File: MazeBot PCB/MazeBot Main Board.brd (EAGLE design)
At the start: 74.9 x 45.4 mm, 43 parts, among them IC1 7805TV, IC2 L298, Q1 16MHz

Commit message: Add mounting screw holes
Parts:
- moved MOT_R 1.27 mm to (64.8, 40.6)
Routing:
- net MOT2_R: track 51.3 -> 48.6 mm
- net MOT1_R: track 48.1 -> 47.6 mm
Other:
- board size 74.9 x 45.4 mm -> 76.2 x 45.4 mm
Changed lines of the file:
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@@
 <layer number="43" name="vRestrict" color="2" fill="10" visible="yes" active="yes"/>
 <layer number="44" name="Drills" color="7" fill="1" visible="no" active="yes"/>
-<layer number="45" name="Holes" color="7" fill="1" visible="no" active="yes"/>
+<layer number="45" name="Holes" color="7" fill="1" visible="yes" active="yes"/>
 <layer number="46" name="Milling" color="3" fill="1" visible="no" active="yes"/>
 <layer number="47" name="Measures" color="7" fill="1" visible="no" active="yes"/>
@@
 <board>
 <plain>
-<wire x1="0" y1="0" x2="74.91" y2="0" width="0" layer="20"/>
-<wire x1="74.91" y1="0" x2="74.91" y2="45.39" width="0" layer="20"/>
-<wire x1="74.91" y1="45.39" x2="0" y2="45.39" width="0" layer="20"/>
+<wire x1="0" y1="0" x2="76.18" y2="0" width="0" layer="20"/>
+<wire x1="76.18" y1="0" x2="76.18" y2="45.39" width="0" layer="20"/>
+<wire x1="76.18" y1="45.39" x2="0" y2="45.39" width="0" layer="20"/>
 <wire x1="0" y1="45.39" x2="0" y2="0" width="0" layer="20"/>
+<hole x="2.54" y="3.81" drill="3.5"/>
+<hole x="2.54" y="41.91" drill="3.5"/>
+<hole x="73.66" y="3.81" drill="3.5"/>
+<hole x="73.66" y="42.164" drill="3.5"/>
 </plain>
 <attributes>
@@
 <attribute name="NAME" x="6.27" y="37.64" size="1.27" layer="25" rot="R90"/>
 </element>
-<element name="MOT_R" library="adafruit" package="1X2-3.5MM" value="1X2-3.5MM" x="63.5" y="40.64" smashed="yes" rot="R180">
-<attribute name="NAME" x="67.39" y="43.64" size="1.27" layer="25" rot="R270"/>
+<element name="MOT_R" library="adafruit" package="1X2-3.5MM" value="1X2-3.5MM" x="64.77" y="40.64" smashed="yes" rot="R180">
+<attribute name="NAME" x="68.66" y="43.64" size="1.27" layer="25" rot="R270"/>
 </element>
 <element name="PWR_IN" library="adafruit" package="1X2-3.5MM" value="1X2-3.5MM" x="35.56" y="40.64" smashed="yes" rot="R180">
@@
 <contactref element="C11" pad="-"/>
 <contactref element="PWR_IN" pad="1"/>
-<polygon width="0.4064" layer="1" isolate="0.3048">
-<vertex x="0" y="45.72"/>
-<vertex x="0" y="0"/>
-<vertex x="74.93" y="0"/>
-<vertex x="74.93" y="44.45"/>
-<vertex x="74.93" y="45.72"/>
-</polygon>
-<polygon width="0.4064" layer="16" isolate="0.3048">
-<vertex x="0" y="45.72"/>
-<vertex x="0" y="0"/>
-<vertex x="74.93" y="0"/>
-<vertex x="74.93" y="45.72"/>
-</polygon>
 <via x="44.958" y="19.939" extent="1-16" drill="0.35"/>
 <via x="49.53" y="18.669" extent="1-16" drill="0.35"/>
@@
 <via x="65.278" y="38.608" extent="1-16" drill="0.35"/>
 <via x="57.15" y="26.924" extent="1-16" drill="0.35"/>
+<polygon width="0.508" layer="1" isolate="0.3048">
+<vertex x="0" y="45.72"/>
+<vertex x="0" y="0"/>
+<vertex x="76.2" y="0"/>
+<vertex x="76.2" y="44.45"/>
+<vertex x="76.2" y="45.72"/>
+</polygon>
+<polygon width="0.508" layer="16" isolate="0.3048">
+<vertex x="0" y="45.72"/>
+<vertex x="0" y="0"/>
+<vertex x="76.2" y="0"/>
+<vertex x="76.2" y="45.72"/>
+</polygon>
+<wire x1="42.418" y1="30.734" x2="40.03" y2="29.93" width="0" layer="19" extent="1-1"/>
+<wire x1="42.63" y1="20.13" x2="44.958" y2="19.939" width="0" layer="19" extent="1-1"/>
+<wire x1="35.23" y1="18.33" x2="31.877" y2="16.891" width="0" layer="19" extent="1-1"/>
 </signal>
 <signal name="EN_L">
@@
 <wire x1="58.42" y1="6.35" x2="60.47" y2="4.3" width="0.6096" layer="1"/>
 <wire x1="60.47" y1="2.54" x2="65.26" y2="2.54" width="0.6096" layer="1"/>
-<wire x1="61.7" y1="40.64" x2="63.5" y2="38.84" width="0.8128" layer="16"/>
-<wire x1="63.5" y1="38.84" x2="63.5" y2="13.97" width="0.8128" layer="16"/>
+<wire x1="62.97" y1="40.64" x2="63.5" y2="40.11" width="0.8128" layer="16"/>
+<wire x1="63.5" y1="40.11" x2="63.5" y2="13.97" width="0.8128" layer="16"/>
 <wire x1="63.5" y1="13.97" x2="62.23" y2="12.7" width="0.8128" layer="16"/>
 <wire x1="62.23" y1="12.7" x2="60.96" y2="12.7" width="0.8128" layer="16"/>
@@
 <wire x1="66.04" y1="10.16" x2="66.04" y2="11.43" width="0.6096" layer="1"/>
 <wire x1="60.47" y1="7.62" x2="64.77" y2="7.62" width="0.6096" layer="1"/>
-<wire x1="71.12" y1="40.64" x2="73.4876" y2="38.2724" width="0.8128" layer="1"/>
+<wire x1="68.58" y1="40.64" x2="73.4876" y2="35.7324" width="0.8128" layer="1"/>
 <wire x1="73.4876" y1="12.5276" x2="72.39" y2="11.43" width="0.8128" layer="1"/>
 <wire x1="72.39" y1="11.43" x2="66.04" y2="11.43" width="0.8128" layer="1"/>
-<wire x1="65.2" y1="40.64" x2="71.12" y2="40.64" width="0.8128" layer="1"/>
-<wire x1="73.4876" y1="38.2724" x2="73.4876" y2="12.5276" width="0.8128" layer="1"/>
+<wire x1="66.47" y1="40.64" x2="68.58" y2="40.64" width="0.8128" layer="1"/>
+<wire x1="73.4876" y1="35.7324" x2="73.4876" y2="12.5276" width="0.8128" layer="1"/>
 <wire x1="64.77" y1="7.62" x2="65.26" y2="7.62" width="0" layer="19" extent="1-1"/>
 </signal>

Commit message: Fix ground connections
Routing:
- net GND: track 4.87 -> 14.9 mm
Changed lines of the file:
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@@
 <vertex x="76.2" y="45.72"/>
 </polygon>
-<wire x1="42.418" y1="30.734" x2="40.03" y2="29.93" width="0" layer="19" extent="1-1"/>
-<wire x1="42.63" y1="20.13" x2="44.958" y2="19.939" width="0" layer="19" extent="1-1"/>
-<wire x1="35.23" y1="18.33" x2="31.877" y2="16.891" width="0" layer="19" extent="1-1"/>
+<wire x1="42.418" y1="30.734" x2="41.91" y2="31.242" width="0.508" layer="1"/>
+<wire x1="41.91" y1="31.242" x2="40.513" y2="31.242" width="0.508" layer="1"/>
+<wire x1="40.513" y1="31.242" x2="40.03" y2="30.759" width="0.508" layer="1"/>
+<wire x1="40.03" y1="30.759" x2="40.03" y2="29.93" width="0.508" layer="1"/>
+<wire x1="33.02" y1="15.24" x2="35.23" y2="17.45" width="0.508" layer="1"/>
+<wire x1="35.23" y1="17.45" x2="35.23" y2="18.33" width="0.508" layer="1"/>
+<wire x1="42.63" y1="20.13" x2="44.767" y2="20.13" width="0.508" layer="1"/>
+<wire x1="44.767" y1="20.13" x2="44.958" y2="19.939" width="0.508" layer="1"/>
 </signal>
 <signal name="EN_L">

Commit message: Fix DRC
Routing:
- net GND: vias 69 -> 70

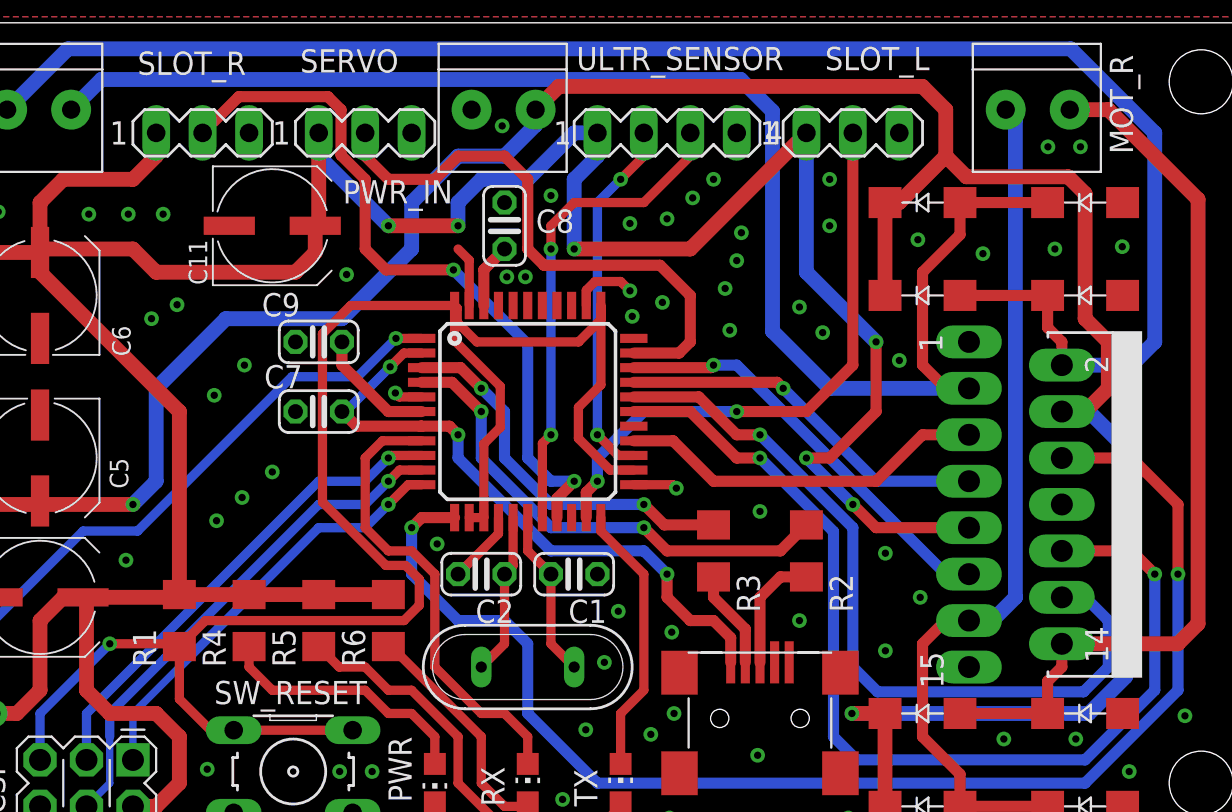
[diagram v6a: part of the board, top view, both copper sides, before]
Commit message: Fix libraries nums on pads
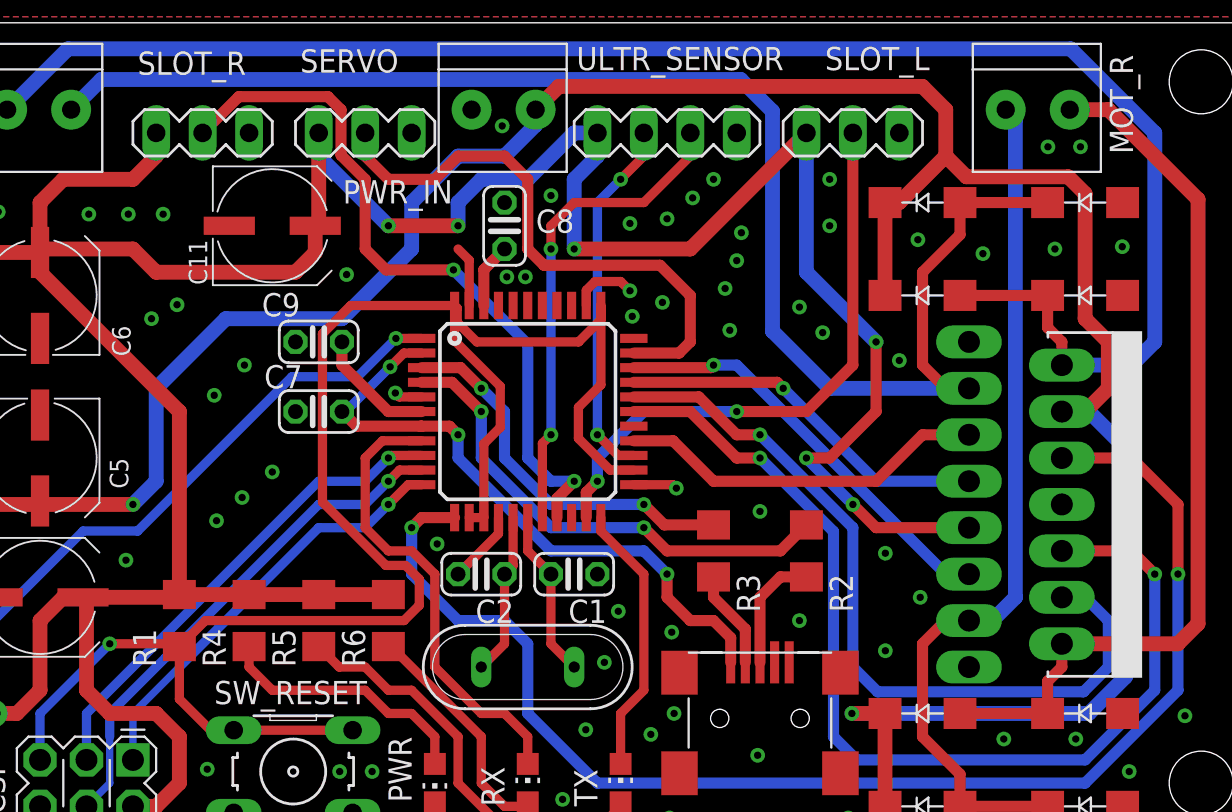
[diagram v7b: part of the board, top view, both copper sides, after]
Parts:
- IC2: device st-microelectronics:MULTIWATT-15 -> EAGLE_std_edits_MZ:MULTIWATT-15
- SERVO, SLOT_L, SLOT_R: device con-lstb:MA03-1 -> EAGLE_std_edits_MZ:MA03-1
- ULTR_SENSOR: device con-lstb:MA04-1 -> EAGLE_std_edits_MZ:MA04-1
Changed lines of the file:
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@@
 <attribute name="VALUE" x="8.89" y="20.32" size="1.27" layer="27" ratio="10" rot="R90" display="off"/>
 </element>
-<element name="IC2" library="st-microelectronics" library_urn="urn:adsk.eagle:library:368" package="MULTIWATT-15" package3d_urn="urn:adsk.eagle:package:26823/1" value="L298" x="68.58" y="19.05" smashed="yes" rot="R270">
+<element name="IC2" library="EAGLE_std_edits_MZ" package="MULTIWATT-15" package3d_urn="urn:adsk.eagle:package:26823/1" value="L298" x="68.58" y="19.05" smashed="yes" rot="R270">
 <attribute name="MF" value="" x="54.61" y="-29.21" size="1.778" layer="27" rot="R270" display="off"/>
 <attribute name="MPN" value="L298N" x="54.61" y="-29.21" size="1.778" layer="27" rot="R270" display="off"/>
@@
 <attribute name="VALUE" x="39.37" y="2.54" size="1.27" layer="27" rot="R90"/>
 </element>
-<element name="SERVO" library="con-lstb" library_urn="urn:adsk.eagle:library:162" package="MA03-1" package3d_urn="urn:adsk.eagle:package:8339/1" value="" x="27.94" y="39.37" smashed="yes">
+<element name="SERVO" library="EAGLE_std_edits_MZ" package="MA03-1" package3d_urn="urn:adsk.eagle:package:8339/1" value="" x="27.94" y="39.37" smashed="yes">
 <attribute name="MF" value="" x="76.2" y="-26.67" size="1.778" layer="27" display="off"/>
 <attribute name="MPN" value="" x="76.2" y="-26.67" size="1.778" layer="27" display="off"/>
@@
 <attribute name="VALUE" x="24.13" y="36.449" size="1.27" layer="27" ratio="10"/>
 </element>
-<element name="SLOT_L" library="con-lstb" library_urn="urn:adsk.eagle:library:162" package="MA03-1" package3d_urn="urn:adsk.eagle:package:8339/1" value="" x="54.61" y="39.37" smashed="yes">
+<element name="SLOT_L" library="EAGLE_std_edits_MZ" package="MA03-1" package3d_urn="urn:adsk.eagle:package:8339/1" value="" x="54.61" y="39.37" smashed="yes">
 <attribute name="MF" value="" x="92.71" y="-26.67" size="1.778" layer="27" display="off"/>
 <attribute name="MPN" value="" x="92.71" y="-26.67" size="1.778" layer="27" display="off"/>
@@
 <attribute name="VALUE" x="50.8" y="36.449" size="1.27" layer="27" ratio="10"/>
 </element>
-<element name="SLOT_R" library="con-lstb" library_urn="urn:adsk.eagle:library:162" package="MA03-1" package3d_urn="urn:adsk.eagle:package:8339/1" value="" x="19.05" y="39.37" smashed="yes">
+<element name="SLOT_R" library="EAGLE_std_edits_MZ" package="MA03-1" package3d_urn="urn:adsk.eagle:package:8339/1" value="" x="19.05" y="39.37" smashed="yes">
 <attribute name="MF" value="" x="41.91" y="-26.67" size="1.778" layer="27" display="off"/>
 <attribute name="MPN" value="" x="41.91" y="-26.67" size="1.778" layer="27" display="off"/>
@@
 <attribute name="VALUE" x="32.385" y="15.3749" size="1.778" layer="27" display="off"/>
 </element>
-<element name="ULTR_SENSOR" library="con-lstb" library_urn="urn:adsk.eagle:library:162" package="MA04-1" package3d_urn="urn:adsk.eagle:package:8337/1" value="" x="44.45" y="39.37" smashed="yes">
+<element name="ULTR_SENSOR" library="EAGLE_std_edits_MZ" package="MA04-1" package3d_urn="urn:adsk.eagle:package:8337/1" value="" x="44.45" y="39.37" smashed="yes">
 <attribute name="MF" value="" x="99.06" y="-20.32" size="1.778" layer="27" display="off"/>
 <attribute name="MPN" value="" x="99.06" y="-20.32" size="1.778" layer="27" display="off"/>
